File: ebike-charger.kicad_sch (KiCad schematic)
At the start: 0 parts

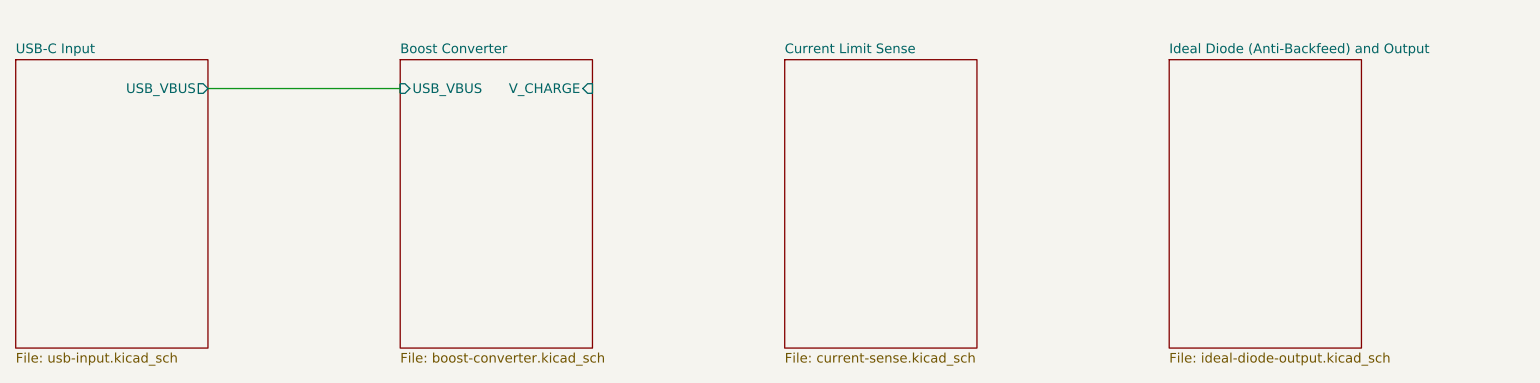
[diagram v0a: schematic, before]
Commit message: added ideal diode
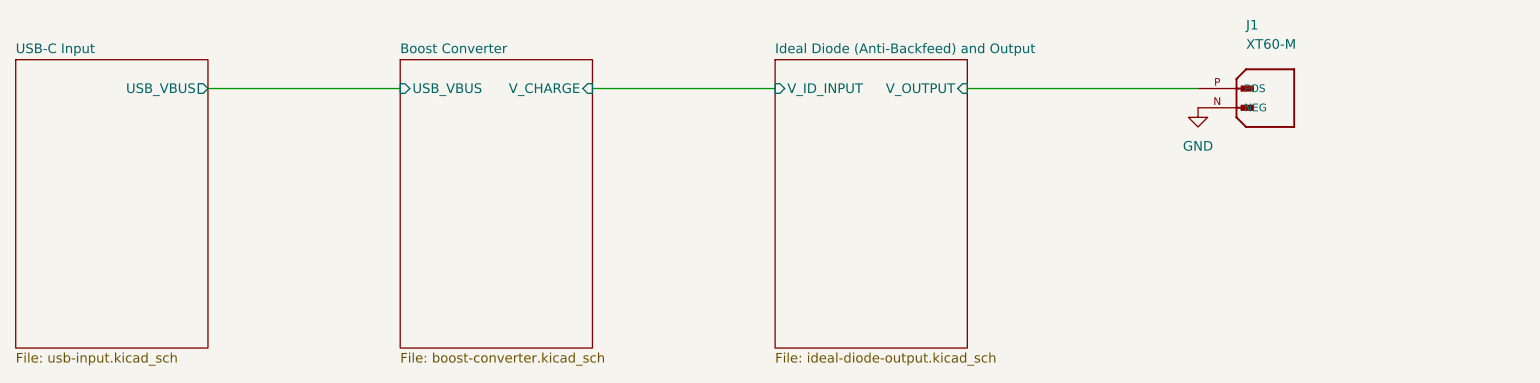
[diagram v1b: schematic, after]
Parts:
- added J1: XT60-M, Snapeda:XT60-M_AMASS_XT60-M, symbol Snapeda:XT60-M
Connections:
- new net GND: J1.N (NEG)
- new net Ideal Diode (Anti-Backfeed) and Output/V_OUTPUT: J1.P (POS)
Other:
- removed sheet Current Limit Sense
- sheet Ideal Diode (Anti-Backfeed) and Output ports: added V_ID_INPUT, V_OUTPUT; removed none
